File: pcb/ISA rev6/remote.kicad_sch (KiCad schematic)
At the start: 20 parts, among them J1 SATA RH Connector, J2 Generic Connector, J3 PiOLED Connector, J4 Qwiic/STEMMA QT, J5 User Controllable GPIO, SW1 Up, SW2 Down, SW3 Select, SW4 Back, U1 AMS1117-3.3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

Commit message: PCB rev 6 part deux
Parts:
- removed J5: User Controllable GPIO, Connector_PinHeader_2.54mm:PinHeader_1x05_P2.54mm_Vertical, symbol Connector:Conn_01x05_Female
- added J5: Config Jumpers, Connector_PinSocket_1.27mm:PinSocket_2x03_P1.27mm_Vertical_SMD, symbol Connector_Generic:Conn_02x03_Odd_Even
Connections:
- net +3V3: now also J5.2 (Pin_2), J5.4 (Pin_4), J5.6 (Pin_6)
- net at U2.13 (GP5): now also J5.1 (Pin_1)
- net at U2.14 (GP6): now also J5.3 (Pin_3)
- net at U2.15 (GP7): now also J5.5 (Pin_5)
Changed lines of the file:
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@@
   (title_block
     (title "PicoPOST Remote")
-    (date "2022-12-30")
+    (date "2023-01-01")
     (rev "0.2")
     (company "The Retro Web")
@@
   (junction (at 76.2 97.79) (diameter 0) (color 0 0 0 0)
   )
+  (junction (at 140.97 125.73) (diameter 0) (color 0 0 0 0)
+  )
   (junction (at 88.9 97.79) (diameter 0) (color 0 0 0 0)
   )
+  (wire (pts (xy 139.7 128.27) (xy 140.97 128.27))
+    (stroke (width 0) (type default) (color 0 0 0 0))
+  )
+  (wire (pts (xy 140.97 123.19) (xy 140.97 125.73))
+    (stroke (width 0) (type default) (color 0 0 0 0))
+  )
   (polyline (pts (xy 25.4 190.5) (xy 101.6 190.5))
     (stroke (width 0) (type default) (color 0 0 0 0))
   )
+  (wire (pts (xy 140.97 128.27) (xy 140.97 125.73))
+    (stroke (width 0) (type default) (color 0 0 0 0))
+  )
   (wire (pts (xy 50.8 123.19) (xy 127 123.19))
     (stroke (width 0) (type default) (color 0 0 0 0))
@@
     (stroke (width 0) (type default) (color 0 0 0 0))
   )
+  (wire (pts (xy 139.7 125.73) (xy 140.97 125.73))
+    (stroke (width 0) (type default) (color 0 0 0 0))
+  )
   (wire (pts (xy 114.3 97.79) (xy 114.3 102.87))
     (stroke (width 0) (type default) (color 0 0 0 0))
@@
   )
   (wire (pts (xy 114.3 120.65) (xy 114.3 107.95))
+    (stroke (width 0) (type default) (color 0 0 0 0))
+  )
+  (wire (pts (xy 139.7 123.19) (xy 140.97 123.19))
     (stroke (width 0) (type default) (color 0 0 0 0))
   )
@@
     )
     (pin "1")
+  )
+  (symbol (lib_id "Connector_Generic:Conn_02x03_Odd_Even") (at 132.08 125.73 0) (unit 1)
+    (in_bom yes) (on_board yes) (fields_autoplaced)
+    (property "Reference" "J5" (id 0) (at 133.35 118.2202 0))
+    (property "Value" "Config Jumpers" (id 1) (at 133.35 120.7571 0))
+    (property "Footprint" "Connector_PinSocket_1.27mm:PinSocket_2x03_P1.27mm_Vertical_SMD" (id 2) (at 132.08 125.73 0)
+      (effects (font (size 1.27 1.27)) hide)
+    )
+    (property "Datasheet" "~" (id 3) (at 132.08 125.73 0)
+      (effects (font (size 1.27 1.27)) hide)
+    )
+    (pin "1")
+    (pin "2")
+    (pin "3")
+    (pin "4")
+    (pin "5")
+    (pin "6")
   )
   (symbol (lib_id "Mechanical:MountingHole") (at 149.86 34.29 0) (unit 1)
@@
     (pin "1")
   )
-  (symbol (lib_id "power:+3.3V") (at 127 130.81 90) (unit 1)
-    (in_bom yes) (on_board yes) (fields_autoplaced)
-    (property "Reference" "#PWR0101" (id 0) (at 130.81 130.81 0)
-      (effects (font (size 1.27 1.27)) hide)
-    )
-    (property "Value" "+3.3V" (id 1) (at 123.825 131.2438 90)
-      (effects (font (size 1.27 1.27)) (justify left))
-    )
-    (property "Footprint" "" (id 2) (at 127 130.81 0)
-      (effects (font (size 1.27 1.27)) hide)
-    )
-    (property "Datasheet" "" (id 3) (at 127 130.81 0)
+  (symbol (lib_id "power:+3.3V") (at 140.97 125.73 270) (unit 1)
+    (in_bom yes) (on_board yes) (fields_autoplaced)
+    (property "Reference" "#PWR0101" (id 0) (at 137.16 125.73 0)
+      (effects (font (size 1.27 1.27)) hide)
+    )
+    (property "Value" "+3.3V" (id 1) (at 144.145 126.1638 90)
+      (effects (font (size 1.27 1.27)) (justify left))
+    )
+    (property "Footprint" "" (id 2) (at 140.97 125.73 0)
+      (effects (font (size 1.27 1.27)) hide)
+    )
+    (property "Datasheet" "" (id 3) (at 140.97 125.73 0)
       (effects (font (size 1.27 1.27)) hide)
     )
@@
     (pin "2")
   )
-  (symbol (lib_id "Connector:Conn_01x05_Female") (at 132.08 128.27 0) (unit 1)
-    (in_bom yes) (on_board yes) (fields_autoplaced)
-    (property "Reference" "J5" (id 0) (at 132.7912 127.4353 0)
-      (effects (font (size 1.27 1.27)) (justify left))
-    )
-    (property "Value" "User Controllable GPIO" (id 1) (at 132.7912 129.9722 0)
-      (effects (font (size 1.27 1.27)) (justify left))
-    )
-    (property "Footprint" "Connector_PinHeader_2.54mm:PinHeader_1x05_P2.54mm_Vertical" (id 2) (at 132.08 128.27 0)
-      (effects (font (size 1.27 1.27)) hide)
-    )
-    (property "Datasheet" "~" (id 3) (at 132.08 128.27 0)
-      (effects (font (size 1.27 1.27)) hide)
-    )
-    (pin "1")
-    (pin "2")
-    (pin "3")
-    (pin "4")
-    (pin "5")
-  )
   (symbol (lib_id "power:GND") (at 19.05 110.49 0) (unit 1)
     (in_bom yes) (on_board yes) (fields_autoplaced)
@@
     (pin "1")
     (pin "2")
-  )
-  (symbol (lib_id "power:GND") (at 127 133.35 0) (unit 1)
-    (in_bom yes) (on_board yes) (fields_autoplaced)
-    (property "Reference" "#PWR0102" (id 0) (at 127 139.7 0)
-      (effects (font (size 1.27 1.27)) hide)
-    )
-    (property "Value" "GND" (id 1) (at 127 137.7934 0))
-    (property "Footprint" "" (id 2) (at 127 133.35 0)
-      (effects (font (size 1.27 1.27)) hide)
-    )
-    (property "Datasheet" "" (id 3) (at 127 133.35 0)
-      (effects (font (size 1.27 1.27)) hide)
-    )
-    (pin "1")
   )
   (symbol (lib_id "power:+3V3") (at 55.88 175.26 0) (unit 1)
@@
       (reference "#PWR0101") (unit 1) (value "+3.3V") (footprint "")
     )
-    (path "/a3c36295-3363-4fae-9f82-3e35109a694f"
-      (reference "#PWR0102") (unit 1) (value "GND") (footprint "")
-    )
     (path "/739c6093-b04b-457a-aaf1-ef60eb687859"
       (reference "BZ1") (unit 1) (value "Buzzer") (footprint "modified ICs:7.6mm side mount buzzer")
@@
       (reference "J4") (unit 1) (value "Qwiic/STEMMA QT") (footprint "Connector_JST:JST_SH_SM04B-SRSS-TB_1x04-1MP_P1.00mm_Horizontal")
     )
-    (path "/83f839f9-eb3c-4d0e-932e-19d21ae1e2d8"
-      (reference "J5") (unit 1) (value "User Controllable GPIO") (footprint "Connector_PinHeader_2.54mm:PinHeader_1x05_P2.54mm_Vertical")
+    (path "/359f8846-914d-4a28-8b38-db39c8d8301b"
+      (reference "J5") (unit 1) (value "Config Jumpers") (footprint "Connector_PinSocket_1.27mm:PinSocket_2x03_P1.27mm_Vertical_SMD")
     )
     (path "/b3875f4c-a400-430e-bf11-732cba8801c1"

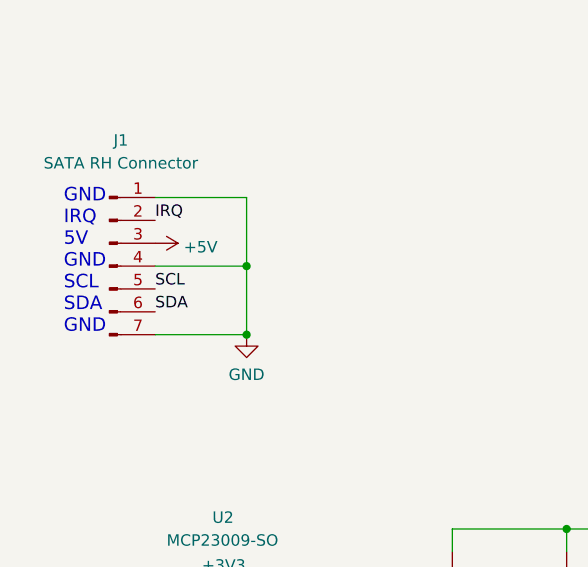
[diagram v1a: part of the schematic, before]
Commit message: [pcb] Fixed pinout mistake on remote connector
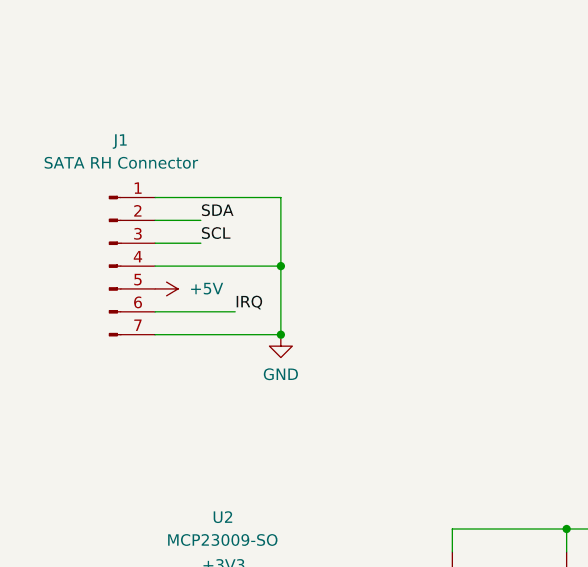
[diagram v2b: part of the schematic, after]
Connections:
- net +5V: now also J1.5 (Pin_5); no longer J1.3 (Pin_3)
- net IRQ: now also J1.6 (Pin_6); no longer J1.2 (Pin_2)
- net SCL: now also J1.3 (Pin_3); no longer J1.5 (Pin_5)
- net SDA: now also J1.2 (Pin_2); no longer J1.6 (Pin_6)
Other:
- note removed: "GND IRQ 5V GND SCL SDA GND"
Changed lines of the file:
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@@
     (comment 1 "by Matthew Petry (fireTwoOneNine) and contributors")
   )
-  (junction (at 40.64 76.2) (diameter 0) (color 0 0 0 0)
-  )
-  (junction (at 40.64 68.58) (diameter 0) (color 0 0 0 0)
-  )
   (junction (at 82.55 97.79) (diameter 0) (color 0 0 0 0)
   )
   (junction (at 68.58 175.26) (diameter 0) (color 0 0 0 0)
   )
+  (junction (at 44.45 76.2) (diameter 0) (color 0 0 0 0)
+  )
   (junction (at 76.2 97.79) (diameter 0) (color 0 0 0 0)
   )
+  (junction (at 44.45 68.58) (diameter 0) (color 0 0 0 0)
+  )
   (junction (at 140.97 125.73) (diameter 0) (color 0 0 0 0)
   )
@@
     (stroke (width 0) (type default) (color 0 0 0 0))
   )
+  (wire (pts (xy 30.48 60.96) (xy 44.45 60.96))
+    (stroke (width 0) (type default) (color 0 0 0 0))
+  )
   (wire (pts (xy 140.97 128.27) (xy 140.97 125.73))
     (stroke (width 0) (type default) (color 0 0 0 0))
   )
+  (wire (pts (xy 30.48 63.5) (xy 35.56 63.5))
+    (stroke (width 0) (type default) (color 0 0 0 0))
+  )
   (wire (pts (xy 50.8 123.19) (xy 127 123.19))
     (stroke (width 0) (type default) (color 0 0 0 0))
@@
     (stroke (width 0) (type default) (color 0 0 0 0))
   )
-  (wire (pts (xy 30.48 60.96) (xy 40.64 60.96))
+  (wire (pts (xy 30.48 73.66) (xy 39.37 73.66))
     (stroke (width 0) (type default) (color 0 0 0 0))
   )
@@
     (stroke (width 0) (type default) (color 0 0 0 0))
   )
-  (wire (pts (xy 40.64 60.96) (xy 40.64 68.58))
+  (wire (pts (xy 44.45 60.96) (xy 44.45 68.58))
     (stroke (width 0) (type default) (color 0 0 0 0))
   )
@@
     (stroke (width 0) (type default) (color 0 0 0 0))
   )
+  (wire (pts (xy 30.48 68.58) (xy 44.45 68.58))
+    (stroke (width 0) (type default) (color 0 0 0 0))
+  )
   (wire (pts (xy 50.8 115.57) (xy 88.9 115.57))
     (stroke (width 0) (type default) (color 0 0 0 0))
@@
     (stroke (width 0) (type default) (color 0 0 0 0))
   )
-  (wire (pts (xy 40.64 68.58) (xy 40.64 76.2))
-    (stroke (width 0) (type default) (color 0 0 0 0))
-  )
   (wire (pts (xy 114.3 120.65) (xy 114.3 107.95))
     (stroke (width 0) (type default) (color 0 0 0 0))
@@
     (stroke (width 0) (type default) (color 0 0 0 0))
   )
+  (wire (pts (xy 30.48 76.2) (xy 44.45 76.2))
+    (stroke (width 0) (type default) (color 0 0 0 0))
+  )
+  (wire (pts (xy 30.48 66.04) (xy 35.56 66.04))
+    (stroke (width 0) (type default) (color 0 0 0 0))
+  )
   (wire (pts (xy 76.2 97.79) (xy 76.2 100.33))
     (stroke (width 0) (type default) (color 0 0 0 0))
@@
     (stroke (width 0) (type default) (color 0 0 0 0))
   )
-  (wire (pts (xy 30.48 68.58) (xy 40.64 68.58))
-    (stroke (width 0) (type default) (color 0 0 0 0))
-  )
   (wire (pts (xy 38.1 172.72) (xy 40.64 172.72))
     (stroke (width 0) (type default) (color 0 0 0 0))
@@
     (stroke (width 0) (type default) (color 0 0 0 0))
   )
-  (wire (pts (xy 30.48 76.2) (xy 40.64 76.2))
-    (stroke (width 0) (type default) (color 0 0 0 0))
-  )
   (wire (pts (xy 50.8 125.73) (xy 127 125.73))
     (stroke (width 0) (type default) (color 0 0 0 0))
@@
     (stroke (width 0) (type default) (color 0 0 0 0))
   )
-  (text "GND\nIRQ\n5V\nGND\nSCL\nSDA\nGND" (at 20.32 76.2 0)
-    (effects (font (size 1.5 1.5)) (justify left bottom))
+  (wire (pts (xy 44.45 68.58) (xy 44.45 76.2))
+    (stroke (width 0) (type default) (color 0 0 0 0))
   )
   (text "Place cap as close to MCP23009 as possible" (at 93.98 21.59 0)
@@
     (effects (font (size 1.27 1.27)) (justify right bottom))
   )
-  (label "SCL" (at 30.48 71.12 0)
-    (effects (font (size 1.27 1.27)) (justify left bottom))
-  )
-  (label "SDA" (at 30.48 73.66 0)
-    (effects (font (size 1.27 1.27)) (justify left bottom))
-  )
   (label "SDA" (at 90.17 177.8 0)
     (effects (font (size 1.27 1.27)) (justify left bottom))
@@
     (effects (font (size 1.27 1.27)) (justify right bottom))
   )
+  (label "IRQ" (at 39.37 73.66 0)
+    (effects (font (size 1.27 1.27)) (justify left bottom))
+  )
+  (label "SCL" (at 35.56 66.04 0)
+    (effects (font (size 1.27 1.27)) (justify left bottom))
+  )
   (label "SCL" (at 55.88 180.34 180)
     (effects (font (size 1.27 1.27)) (justify right bottom))
@@
     (effects (font (size 1.27 1.27)) (justify left bottom))
   )
+  (label "SDA" (at 35.56 63.5 0)
+    (effects (font (size 1.27 1.27)) (justify left bottom))
+  )
   (label "SDA" (at 59.69 30.48 270)
     (effects (font (size 1.27 1.27)) (justify right bottom))
-  )
-  (label "IRQ" (at 30.48 63.5 0)
-    (effects (font (size 1.27 1.27)) (justify left bottom))
   )
   (symbol (lib_id "Connector:Conn_01x07_Male") (at 25.4 68.58 0) (unit 1)
@@
     (pin "1")
   )
-  (symbol (lib_id "power:GND") (at 40.64 76.2 0) (unit 1)
-    (in_bom yes) (on_board yes) (fields_autoplaced)
-    (property "Reference" "#PWR09" (id 0) (at 40.64 82.55 0)
-      (effects (font (size 1.27 1.27)) hide)
-    )
-    (property "Value" "GND" (id 1) (at 40.64 80.6434 0))
-    (property "Footprint" "" (id 2) (at 40.64 76.2 0)
-      (effects (font (size 1.27 1.27)) hide)
-    )
-    (property "Datasheet" "" (id 3) (at 40.64 76.2 0)
+  (symbol (lib_id "power:GND") (at 44.45 76.2 0) (unit 1)
+    (in_bom yes) (on_board yes) (fields_autoplaced)
+    (property "Reference" "#PWR09" (id 0) (at 44.45 82.55 0)
+      (effects (font (size 1.27 1.27)) hide)
+    )
+    (property "Value" "GND" (id 1) (at 44.45 80.6434 0))
+    (property "Footprint" "" (id 2) (at 44.45 76.2 0)
+      (effects (font (size 1.27 1.27)) hide)
+    )
+    (property "Datasheet" "" (id 3) (at 44.45 76.2 0)
       (effects (font (size 1.27 1.27)) hide)
     )
@@
     (pin "1")
   )
-  (symbol (lib_id "power:+5V") (at 30.48 66.04 270) (unit 1)
-    (in_bom yes) (on_board yes) (fields_autoplaced)
-    (property "Reference" "#PWR05" (id 0) (at 26.67 66.04 0)
-      (effects (font (size 1.27 1.27)) hide)
-    )
-    (property "Value" "+5V" (id 1) (at 33.655 66.4738 90)
-      (effects (font (size 1.27 1.27)) (justify left))
-    )
-    (property "Footprint" "" (id 2) (at 30.48 66.04 0)
-      (effects (font (size 1.27 1.27)) hide)
-    )
-    (property "Datasheet" "" (id 3) (at 30.48 66.04 0)
-      (effects (font (size 1.27 1.27)) hide)
-    )
+  (symbol (lib_id "power:+5V") (at 30.48 71.12 270) (mirror x) (unit 1)
+    (in_bom yes) (on_board yes)
+    (property "Reference" "#PWR05" (id 0) (at 26.67 71.12 0)
+      (effects (font (size 1.27 1.27)) hide)
+    )
+    (property "Value" "+5V" (id 1) (at 34.29 71.12 90)
+      (effects (font (size 1.27 1.27)) (justify left))
+    )
+    (property "Footprint" "" (id 2) (at 30.48 71.12 0)
+      (effects (font (size 1.27 1.27)) hide)
+    )
+    (property "Datasheet" "" (id 3) (at 30.48 71.12 0)
+      (effects (font (size 1.27 1.27)) hide)
+    )
